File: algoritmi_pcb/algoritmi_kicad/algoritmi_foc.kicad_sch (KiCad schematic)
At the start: 25 parts, among them IC2 AP2114HA-3.3TRG1, J2 53261-0371, J3 SMM-110-02-H-D-K-TR, U1 TMC6300-LA-T

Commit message: some changes to schematics
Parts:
- removed C9: 10uF 25V, Capacitor_SMD:C_0805_2012Metric, symbol SamacSys_Parts:CL21A106KAYNNNE
- removed IC2: AP2114HA-3.3TRG1, Package_TO_SOT_SMD:SOT-223-3_TabPin2, symbol SamacSys_Parts:AP2114HA-3.3TRG1
- removed J1: ~, solder_pads:solder_pads_2mm_8, symbol solder_pad:solder_pad_2mm_8
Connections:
- net LCD_BL: no longer names the net of J3.12
- net LCD_CLOCK: no longer names the net of J3.4
- net LCD_CS: no longer names the net of J3.6
- net LCD_DATA_IN: no longer names the net of J3.2
- net LCD_DC: no longer names the net of J3.8
- net LCD_RESET: no longer names the net of J3.10
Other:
- note added: "POWER: 5v AND 3v3"
- note removed: "POWER: LDO 3.3V - AP2114HA"
- note removed: "ROUND LCD CONNECTOR 1.28" GC9A01 DRIVER"
- moved on the sheet: J2

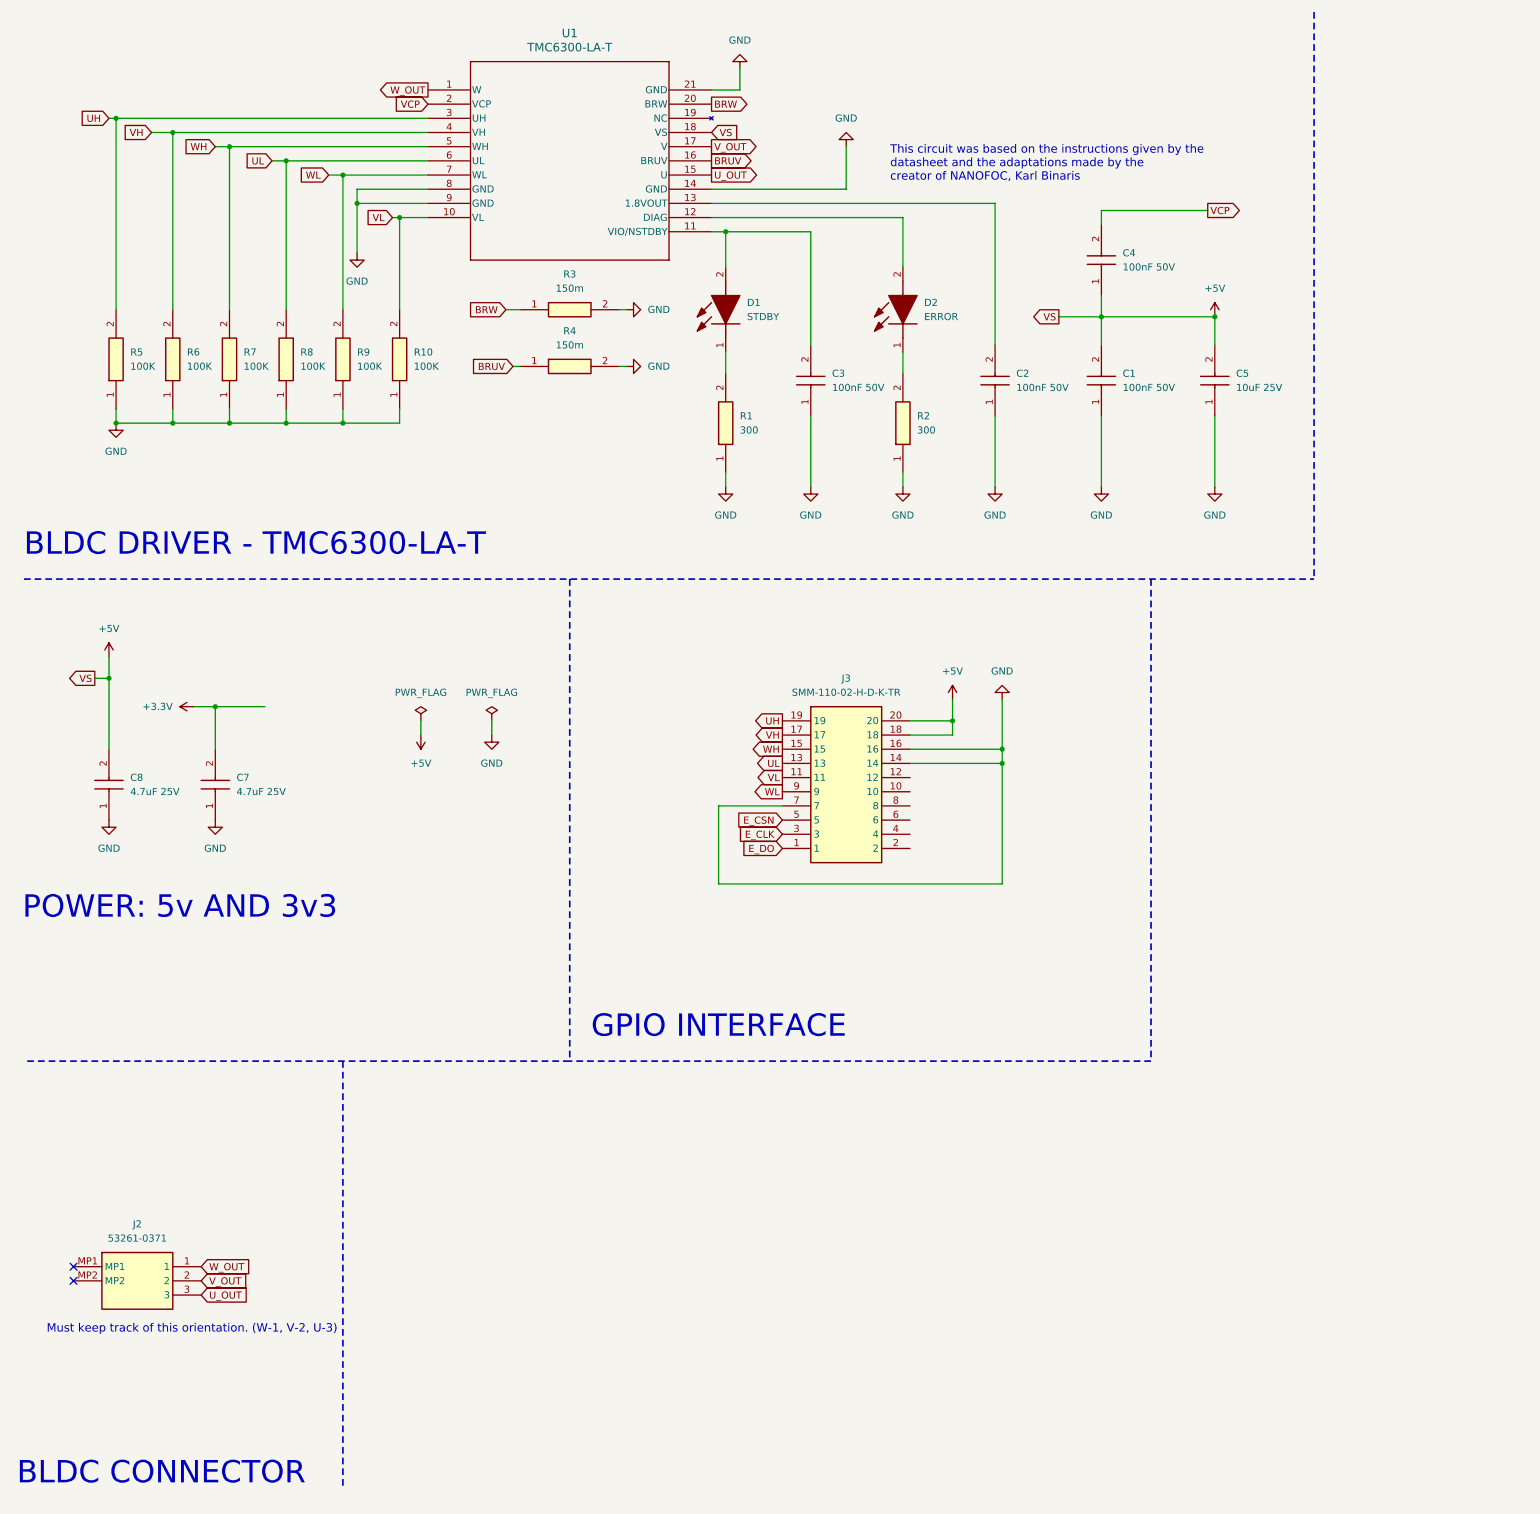
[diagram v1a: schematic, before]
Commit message: updates to the schematics
Updates regarding the schematics: removing power circuits and rechanging some labels and names.
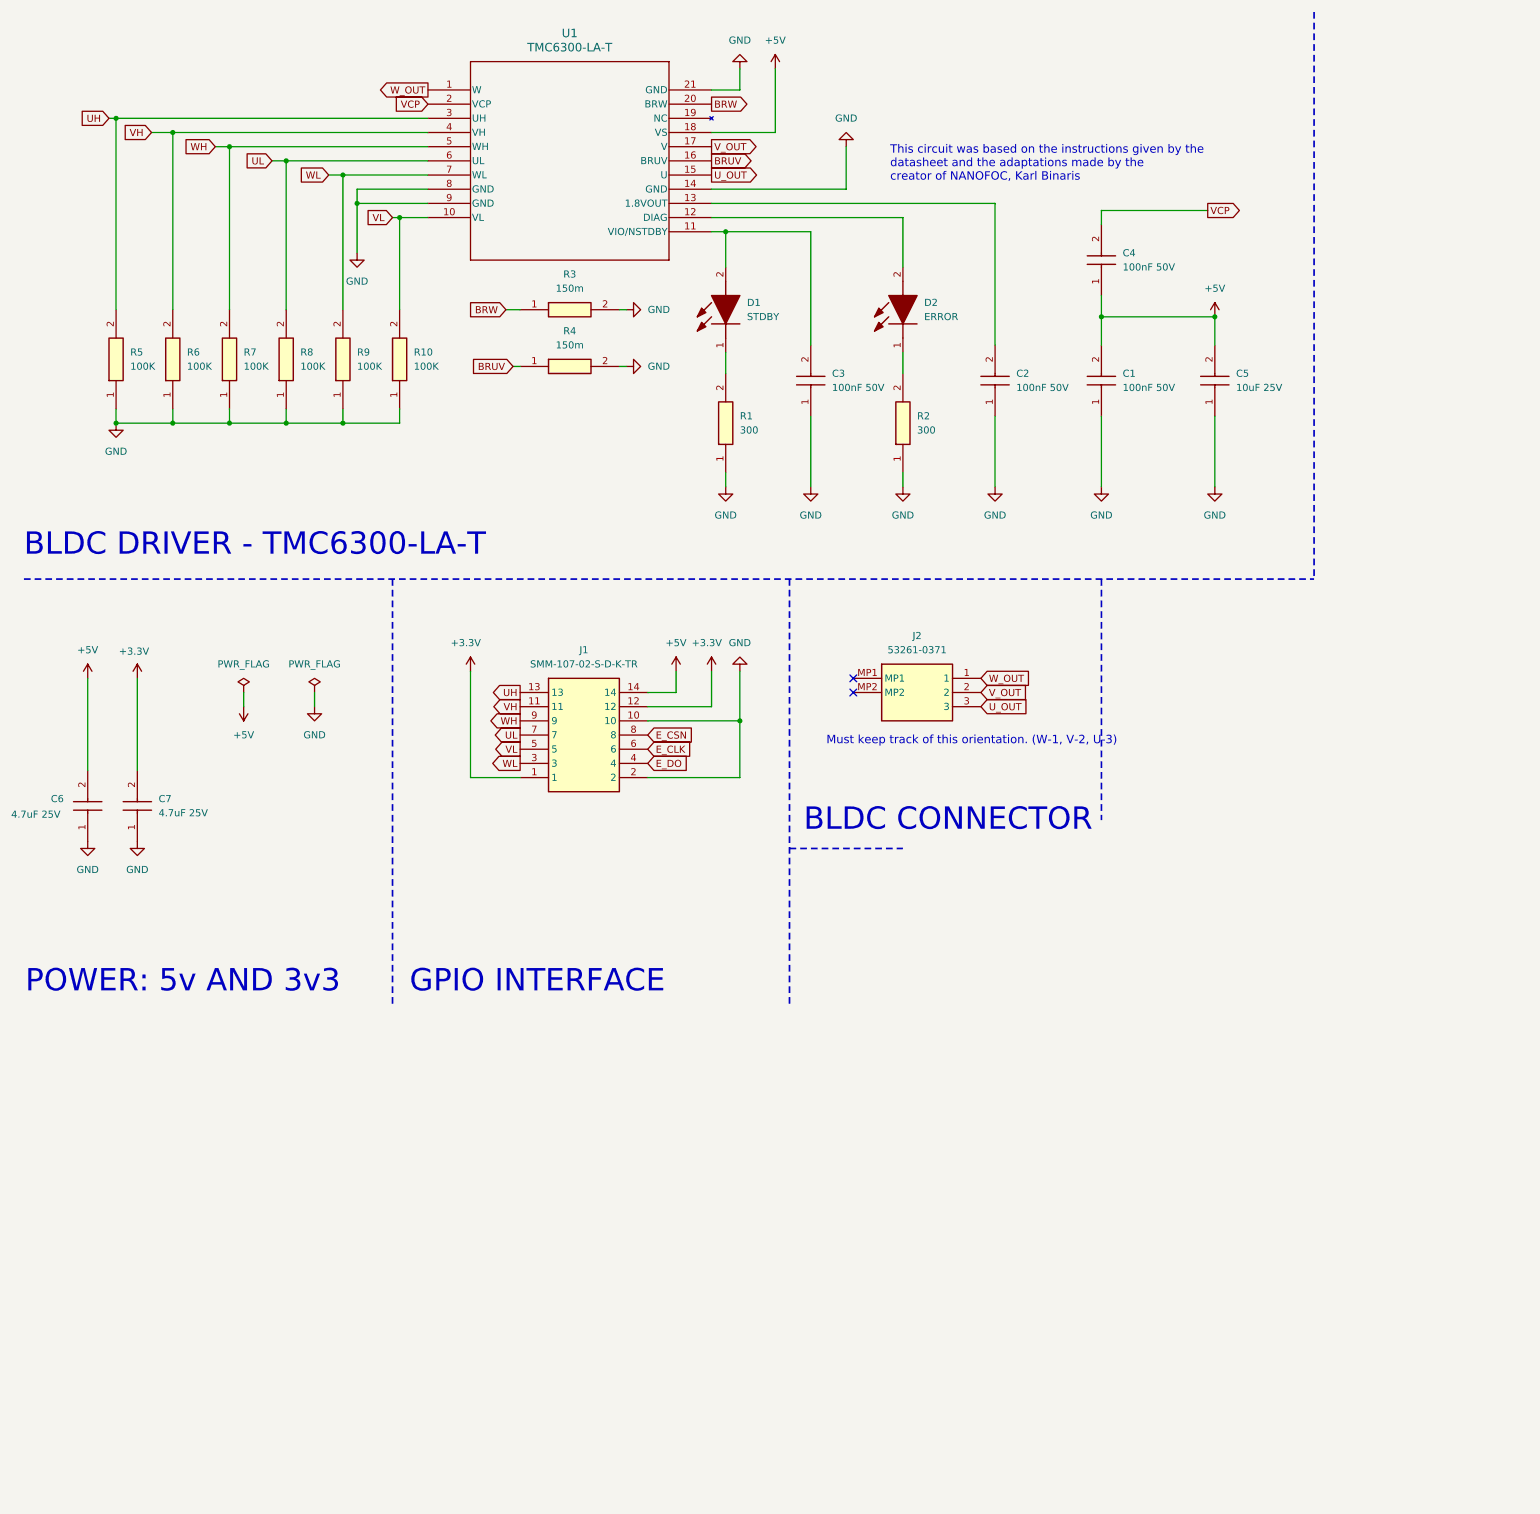
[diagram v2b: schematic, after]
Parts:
- removed C8: 4.7uF 25V, Capacitor_SMD:C_0805_2012Metric, symbol SamacSys_Parts:GCM21BC71E475KE36K
- removed J3: SMM-110-02-H-D-K-TR, SMM-110-02-XX-D-K-TR, symbol SamacSys_Parts:SMM-110-02-H-D-K-TR
- added C6: 4.7uF 25V, Capacitor_SMD:C_0805_2012Metric, symbol SamacSys_Parts:GCM21BC71E475KE36K
- added J1: SMM-107-02-S-D-K-TR, SMM-107-02-XX-D-K-TR, symbol SamacSys_Parts:SMM-107-02-S-D-K-TR
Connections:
- net +3.3V: now also J1.1, J1.12
- net +5V: now also C6.2, J1.14
- net E_CLK: now also J1.6
- net E_CSN: now also J1.8
- net E_DO: now also J1.4
- net GND: now also C6.1, J1.10, J1.2
- net UH: now also J1.13
- net UL: now also J1.7
- net VH: now also J1.11
- net VL: now also J1.5
- net WH: now also J1.9
- net WL: now also J1.3
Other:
- moved on the sheet: C7, J2

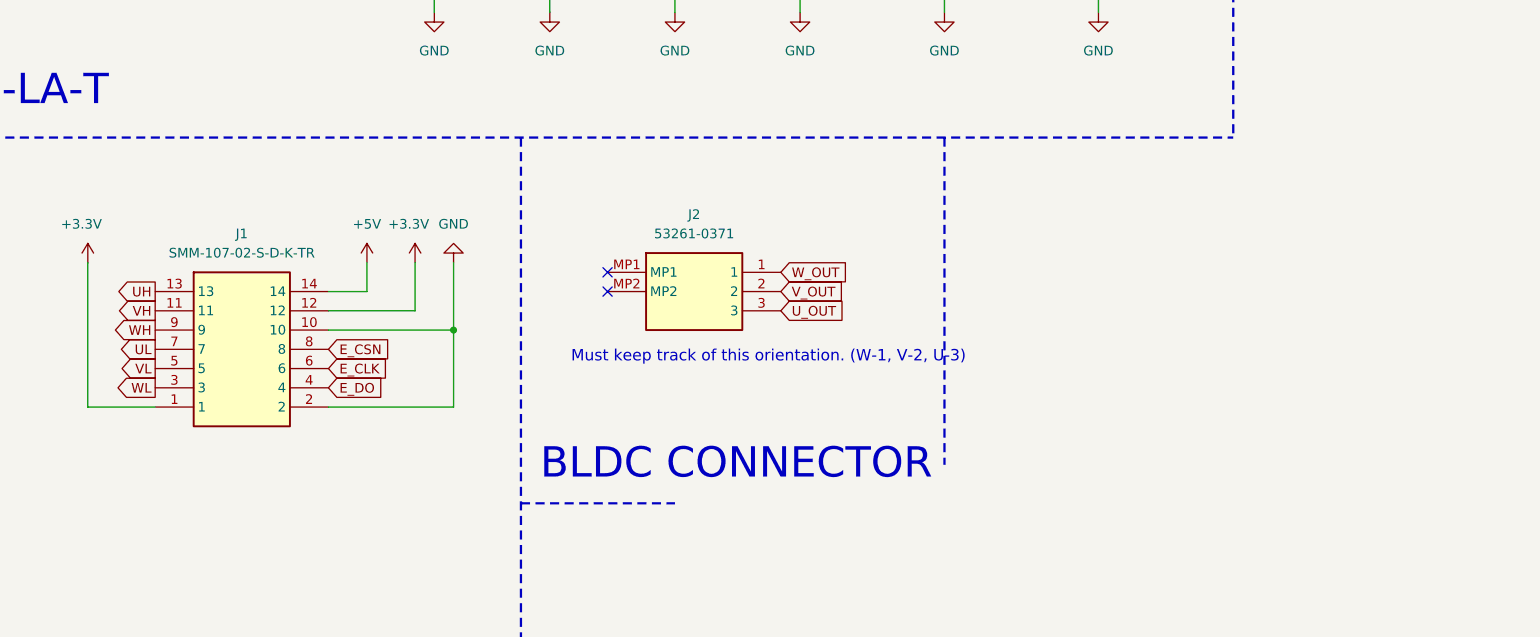
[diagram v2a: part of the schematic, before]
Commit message: Changed the base pcb and started motor pcb
The motor pcb is almost finished, just needs to get the encoder centered in the middle.
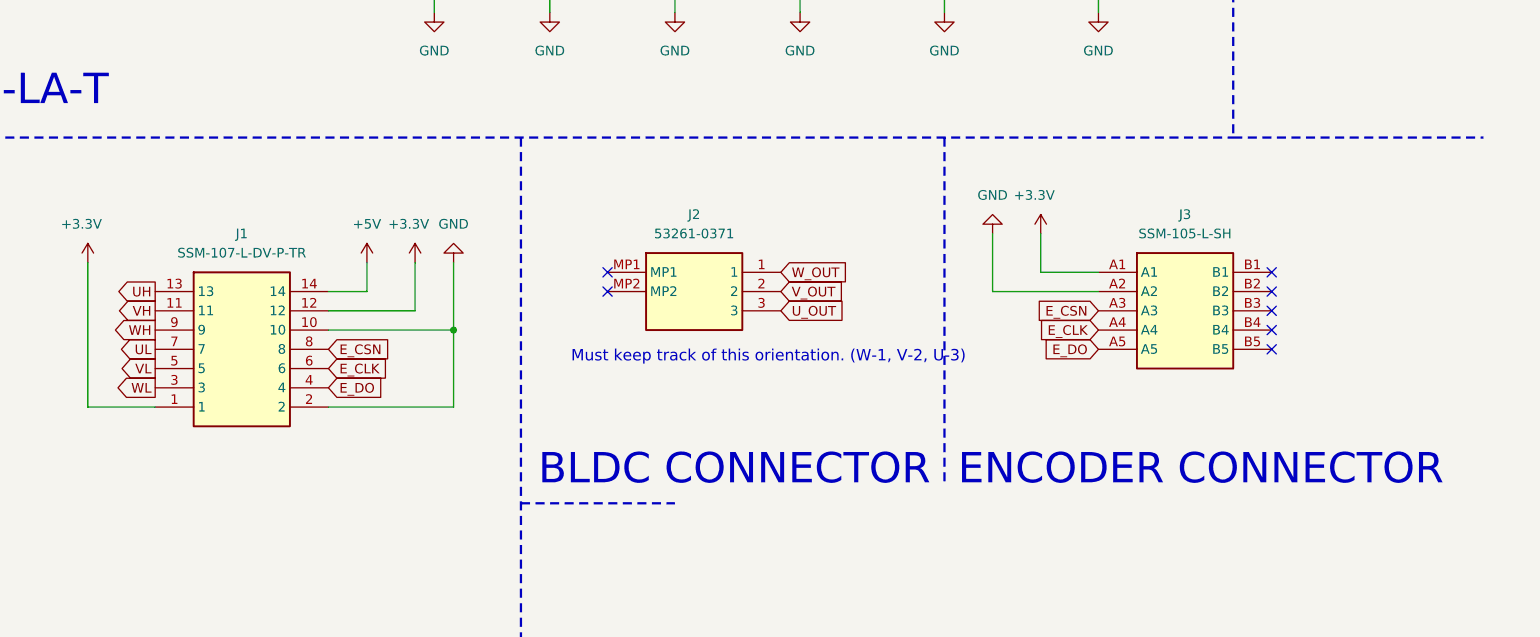
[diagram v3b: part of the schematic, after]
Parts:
- removed J1: SMM-107-02-S-D-K-TR, SMM-107-02-XX-D-K-TR, symbol SamacSys_Parts:SMM-107-02-S-D-K-TR
- added J1: SSM-107-L-DV-P-TR, SSM-107-XXX-DV-P-TR, symbol SamacSys_Parts:SSM-107-L-DV-P-TR
- added J3: SSM-105-L-SH, SSM105LSH, symbol SamacSys_Parts:SSM-105-L-SH
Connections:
- net +3.3V: now also J1.1, J1.12, J3.A1
- net +5V: now also J1.14
- net E_CLK: now also J1.6, J3.A4
- net E_CSN: now also J1.8, J3.A3
- net E_DO: now also J1.4, J3.A5
- net GND: now also J1.10, J1.2, J3.A2
- net UH: now also J1.13
- net UL: now also J1.7
- net VH: now also J1.11
- net VL: now also J1.5
- net WH: now also J1.9
- net WL: now also J1.3
- no-connect marks 2 -> 7
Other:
- note added: "ENCODER CONNECTOR"
